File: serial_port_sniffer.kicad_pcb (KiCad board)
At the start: 2 copper layers, 34 parts, among them J1 DB9_Male_MountingHoles, J10 GS2, J11 Conn_01x01, J12 USB_B, J13 Conn_01x08, J14 Conn_01x03, J15 GS2, J2 DB9_Female_MountingHoles, J3 GS2, J4 GS2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

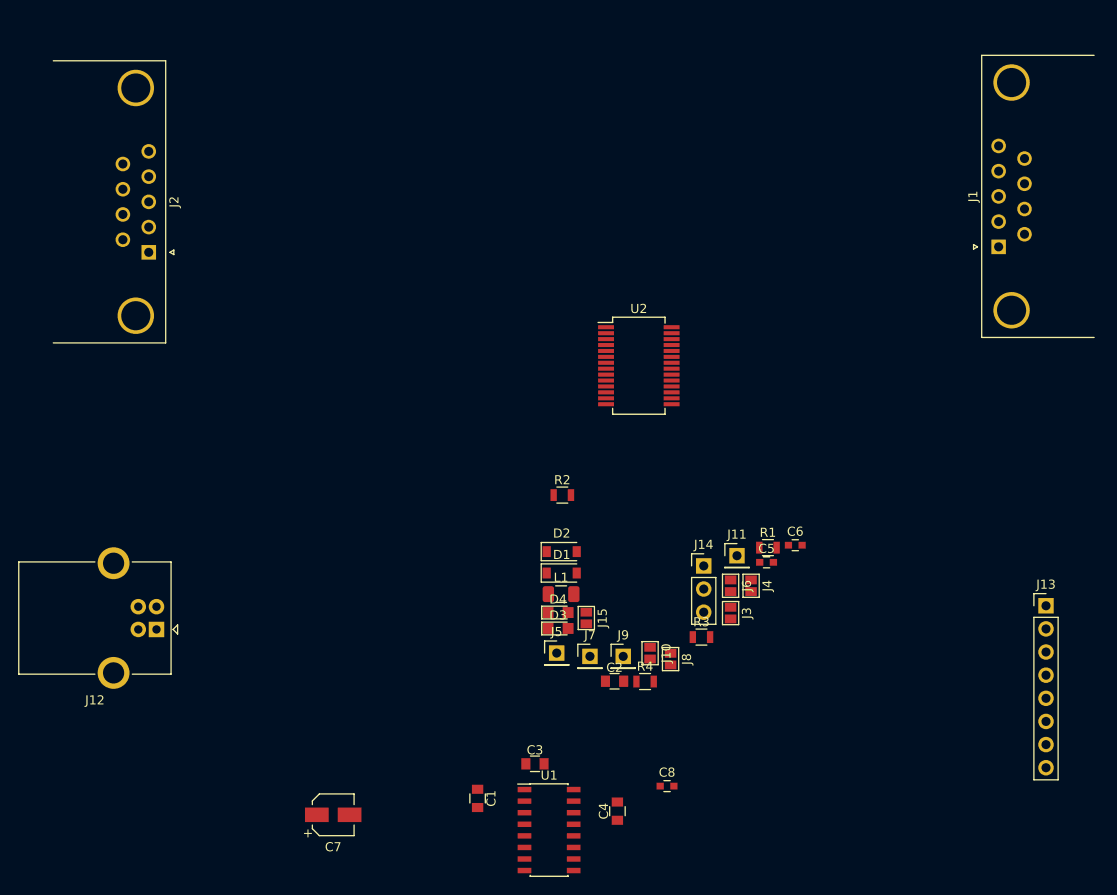
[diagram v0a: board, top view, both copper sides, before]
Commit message: Finished PCB layout
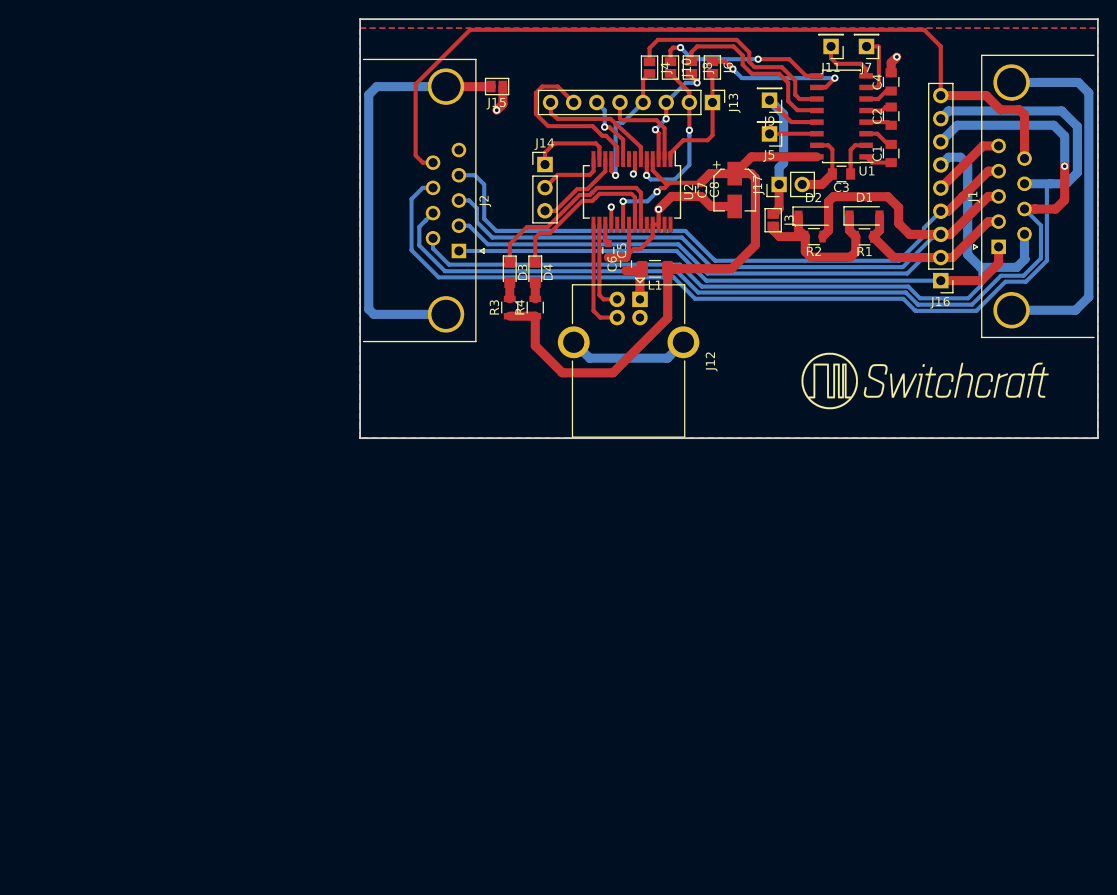
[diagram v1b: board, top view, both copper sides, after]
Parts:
- added G***: LOGO, Switchcraft:Switchcraft_medium_logo, F.Cu at (177.2, 73.7)
- added J16: Conn_01x09, Pin_Headers:Pin_Header_Straight_1x09_Pitch2.54mm, F.Cu at (178.8, 62.7)
- added J17: Conn_01x02, Pin_Headers:Pin_Header_Straight_1x02_Pitch2.54mm, F.Cu at (161.0, 52.1)
- moved C4 85.5 mm to (173.3, 40.9)
- moved U1 84.7 mm to (167.8, 44.7), turned to 180 degrees
- moved C1 84.1 mm to (173.3, 48.8), turned to 90 degrees
- moved C7 81.5 mm to (156.1, 52.8), turned to 270 degrees
- moved J7 73.5 mm to (170.6, 37.0), turned to 180 degrees
- moved C3 73.0 mm to (167.8, 51.0), turned to 180 degrees
- moved C2 69.1 mm to (173.3, 44.6), turned to 90 degrees
- moved J13 66.3 mm to (153.7, 43.1), turned to 270 degrees
- moved C8 65.6 mm to (152.4, 52.7), turned to 270 degrees
- moved J8 65.0 mm to (151.4, 39.3)
- moved J10 64.3 mm to (149.1, 39.3)
- moved J12 64.3 mm to (145.7, 64.8), turned to 270 degrees
- moved J9 63.1 mm to (159.9, 42.9), turned to 180 degrees
- moved J5 61.6 mm to (159.9, 46.6), turned to 180 degrees
- moved J15 59.2 mm to (130.0, 41.4), turned to 270 degrees
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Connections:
- C6 pad 2: Net-(C6-Pad2) -> GND
- J12 pad 4: Net-(C6-Pad2) -> GND
- J3 pad 1: Net-(D1-Pad1) -> Sniffer
- J3 pad 2: Sniffer -> Net-(D1-Pad1)
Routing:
- net Net-(J1-Pad8): track 0.00 -> 119.3 mm
- net Net-(J1-Pad7): track 0.00 -> 110.1 mm, vias 0 -> 1
- net GNDD: track 0.00 -> 100.0 mm
- net Net-(J1-Pad9): track 0.00 -> 91.2 mm
- net Net-(J1-Pad6): track 0.00 -> 89.6 mm
- net Net-(D2-Pad2): track 0.00 -> 85.8 mm
- net VCC: track 0.00 -> 79.8 mm, vias 0 -> 2
- net Net-(D1-Pad2): track 0.00 -> 74.7 mm
- net Net-(J1-Pad4): track 0.00 -> 69.9 mm
- net Net-(J1-Pad1): track 0.00 -> 63.2 mm
- net GND: track 0.00 -> 47.8 mm, vias 0 -> 5
- net Net-(J4-Pad1): track 0.00 -> 24.5 mm
- net Net-(D3-Pad1): track 0.00 -> 22.7 mm
- net Sniffer: track 0.00 -> 19.9 mm
- net Net-(J8-Pad1): track 0.00 -> 19.8 mm
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- added copper zone on B.Cu, net GND
- added copper zone on F.Cu, net GNDD
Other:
- board outline added: 81 x 46 mm
- net class Default: trace_width 0.25 -> 0.45
- net class Power added: clearance 0.2, trace_width 1, via_dia 0.8, via_drill 0.4
- board text added: "RS232 data sniffer. Design by Eirik Haustveit, 2018."
